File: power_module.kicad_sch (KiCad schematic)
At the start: 0 parts

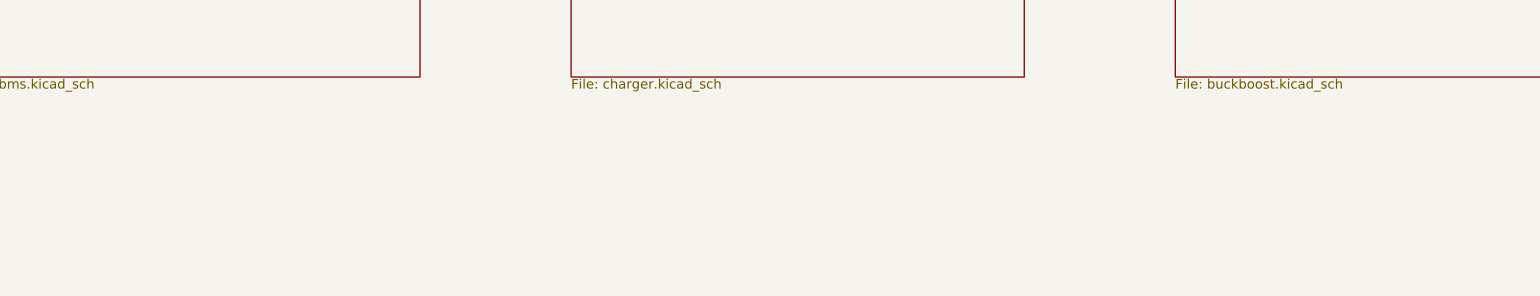
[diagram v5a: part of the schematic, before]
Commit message: schematic: integrate subcircuits — output, I²C, user switch
Top-level power_module.kicad_sch gains the user-facing components:

  J2  Conn_01x02   output header        : V12_OUT, GND
  J3  Conn_01x04   I²C breakout         : SDA, SCL, ALERT, GND
  SW1 SW_SPDT      user on/off switch   : MODULE_EN ↔ BAT+ (pin 3 NC)

For these to span sheets, V12_OUT (Buck-Boost) and SDA/SCL/ALERT (BMS)
were promoted from local labels to global_label inside their child
sheets (one Python pass over each .kicad_sch).  KiCad joins
global_labels by name across all sheets without sheet pins.

User switch behaviour: SW1 routes BAT+ through to a new MODULE_EN
global net.  Inside buckboost.kicad_sch, R23.pin1 (top of the
LM5176 EN/UVLO divider) was switched from BAT+ to MODULE_EN — so
opening SW1 lets R24 pull EN/UVLO low and the buck-boost shuts
down (BMS still runs at its ~10 µA sleep current).

Cleanup: SW1 placeholder in the BMS sheet was deleted (it was
intentionally unwired pending integration; now the real user switch
lives at the parent).

ERC: top-level reports zero errors.  One warning remains
(L_Bourns_SRR1280 footprint not found in default library — pending
the LCSC/footprint-property pass that's still on the to-do list).

Co-Authored-By: Claude Opus 4.7 <noreply@anthropic.com>
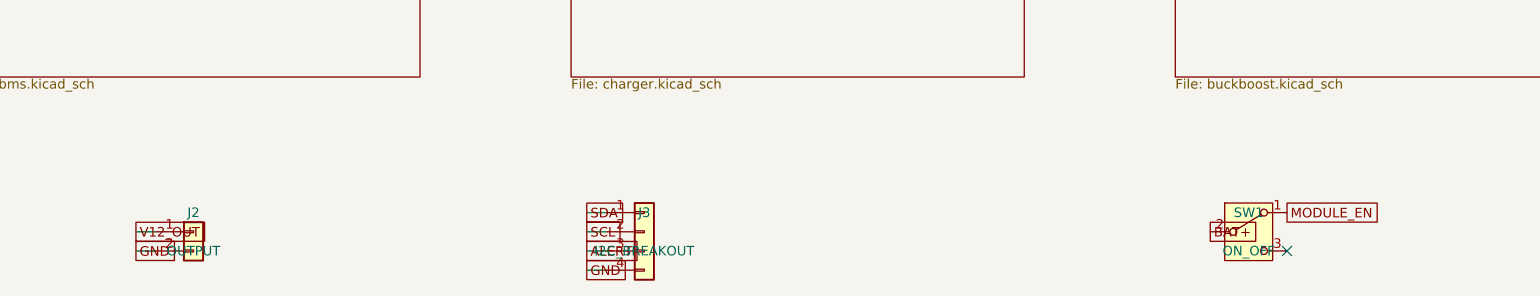
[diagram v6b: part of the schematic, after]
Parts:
- added J2: OUTPUT, Connector_PinHeader_2.54mm:PinHeader_1x02_P2.54mm_Vertical, symbol Connector_Generic:Conn_01x02
- added J3: I2C_BREAKOUT, Connector_PinHeader_2.54mm:PinHeader_1x04_P2.54mm_Vertical, symbol Connector_Generic:Conn_01x04
- added SW1: ON_OFF, Button_Switch_SMD:SW_SPDT_PCM12, symbol Switch:SW_SPDT
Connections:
- new net ALERT: J3.3 (Pin_3)
- new net BAT+: SW1.2 (B)
- new net GND: J2.2 (Pin_2), J3.4 (Pin_4)
- new net MODULE_EN: SW1.1 (A)
- new net SCL: J3.2 (Pin_2)
- new net SDA: J3.1 (Pin_1)
- new net V12_OUT: J2.1 (Pin_1)
- no-connect marks 0 -> 1
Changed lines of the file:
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@@
-(kicad_sch (version 20250114) (generator "KiCAD-MCP-Server")
-  (paper "A4")
-  (sheet (at 50 50) (size 60 40) (fields_autoplaced yes)
-    (stroke (width 0.1524) (type solid))
-    (fill (color 0 0 0 0.0000))
-    (property "Sheetname" "BMS" (at 50 49.8 0)
-      (effects (font (size 1.27 1.27)) (justify left bottom))
-    )
-    (property "Sheetfile" "bms.kicad_sch" (at 50 90.2 0)
-      (effects (font (size 1.27 1.27)) (justify left top))
-    )
-    (instances
-      (project "power_module"
-        (path "/b0f4a1bd-53e2-4ffd-a882-09b61a25e2e6"
-          (page "2")
-        )
-      )
-    )
-  )
-  (sheet (at 130 50) (size 60 40) (fields_autoplaced yes)
-    (stroke (width 0.1524) (type solid))
-    (fill (color 0 0 0 0.0000))
-    (property "Sheetname" "Charger" (at 130 49.8 0)
-      (effects (font (size 1.27 1.27)) (justify left bottom))
-    )
-    (property "Sheetfile" "charger.kicad_sch" (at 130 90.2 0)
-      (effects (font (size 1.27 1.27)) (justify left top))
-    )
-    (instances
-      (project "power_module"
-        (path "/b0f4a1bd-53e2-4ffd-a882-09b61a25e2e6"
-          (page "3")
-        )
-      )
-    )
-  )
-  (sheet (at 210 50) (size 60 40) (fields_autoplaced yes)
-    (stroke (width 0.1524) (type solid))
-    (fill (color 0 0 0 0.0000))
-    (property "Sheetname" "Buck-Boost" (at 210 49.8 0)
-      (effects (font (size 1.27 1.27)) (justify left bottom))
-    )
-    (property "Sheetfile" "buckboost.kicad_sch" (at 210 90.2 0)
-      (effects (font (size 1.27 1.27)) (justify left top))
-    )
-    (instances
-      (project "power_module"
-        (path "/b0f4a1bd-53e2-4ffd-a882-09b61a25e2e6"
-          (page "4")
-        )
-      )
-    )
-  )
-  (sheet_instances
-    (path "/" (page "1"))
-  )
-)
